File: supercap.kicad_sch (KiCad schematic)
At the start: 33 parts, among them Q1001 SS8050, Q1002 SS8050, Q1003 SS8050, U1001 LMV321-TR, U1002 LMV321-TR, U1003 LMV321-TR

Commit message: Weeded out all ERC errors
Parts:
- added C1202: 100nF, Capacitor_SMD:C_0402_1005Metric, symbol Device:C
- added C1206: CHW-2R7206R-TW, Capacitor_THT:CP_Radial_D16.0mm_P7.50mm, symbol Device:C_Polarized
- added D1202: 1N5819WS, Diode_SMD:D_SOD-323_HandSoldering, symbol Device:D_Schottky
- added Q1202: SS8050, Package_TO_SOT_SMD:SOT-23, symbol Transistor_BJT:MMBT5551L
- added R1202: 33k, Resistor_SMD:R_0402_1005Metric, symbol Device:R
- added R1208, R1220: 300k, Resistor_SMD:R_0402_1005Metric, symbol Device:R
- added R1209: 150k, Resistor_SMD:R_0402_1005Metric, symbol Device:R_Small
- added R1210: 120k, Resistor_SMD:R_0402_1005Metric, symbol Device:R_Small
- added R1219: 330k, Resistor_SMD:R_0402_1005Metric, symbol Device:R
- added U1202: LMV321-TR, Package_TO_SOT_SMD:SOT-23-5, symbol Amplifier_Operational:LMV321
- C1004, C1005, C1006: value CAS SCAP 3.0V20F -> CHW-2R7206R-TW; footprint SH-RPi:CP_Radial_D12.6mm_H26.0mm_P5.30mm_Horizontal -> Capacitor_THT:CP_Radial_D16.0mm_P7.50mm
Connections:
- net BO2-: now also R1219.2, R1220.1, U1202.3 (-)
- net BO3+: now also R1208.2, R1209.1, U1202.1 (+); no longer R1004.2, R1005.1, U1001.1 (+)
- net BO3+_: now also R1209.2, R1210.1; no longer R1005.2, R1006.1
- net BO3o: now also Q1202.1 (B), U1202.4; no longer Q1001.1 (B), U1001.4
- net SC23: now also C1202.2, C1206.2, D1202.2 (A), Q1202.2 (E), R1220.2, U1202.2 (V-); no longer C1001.2, C1004.2, D1001.2 (A), Q1001.2 (E), R1014.2, U1001.2 (V-)
- net SC23R: now also R1202.2, R1210.2; no longer R1001.2, R1006.2
- new net BO4+: R1004.2, R1005.1, U1001.1 (+)
- new net BO4+_: R1005.2, R1006.1
- new net BO4o: Q1001.1 (B), U1001.4
- new net SC34: C1001.2, C1004.2, C1202.1, C1206.1, D1001.2 (A), D1202.1 (K), Q1001.2 (E), Q1202.3 (C), R1014.2, R1208.1, U1001.2 (V-), U1202.5 (V+)
- new net SC34R: R1001.2, R1006.2, R1202.1, R1219.1
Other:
- company: Hat Labs Ltd -> Hat Labs Oy
- title: Sailor Hat for Raspberry Pi -> HALPI2
- moved on the sheet: C1001, C1002, C1003, C1004, C1005, C1006, D1001, D1002, D1003, Q1001, Q1002, Q1003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

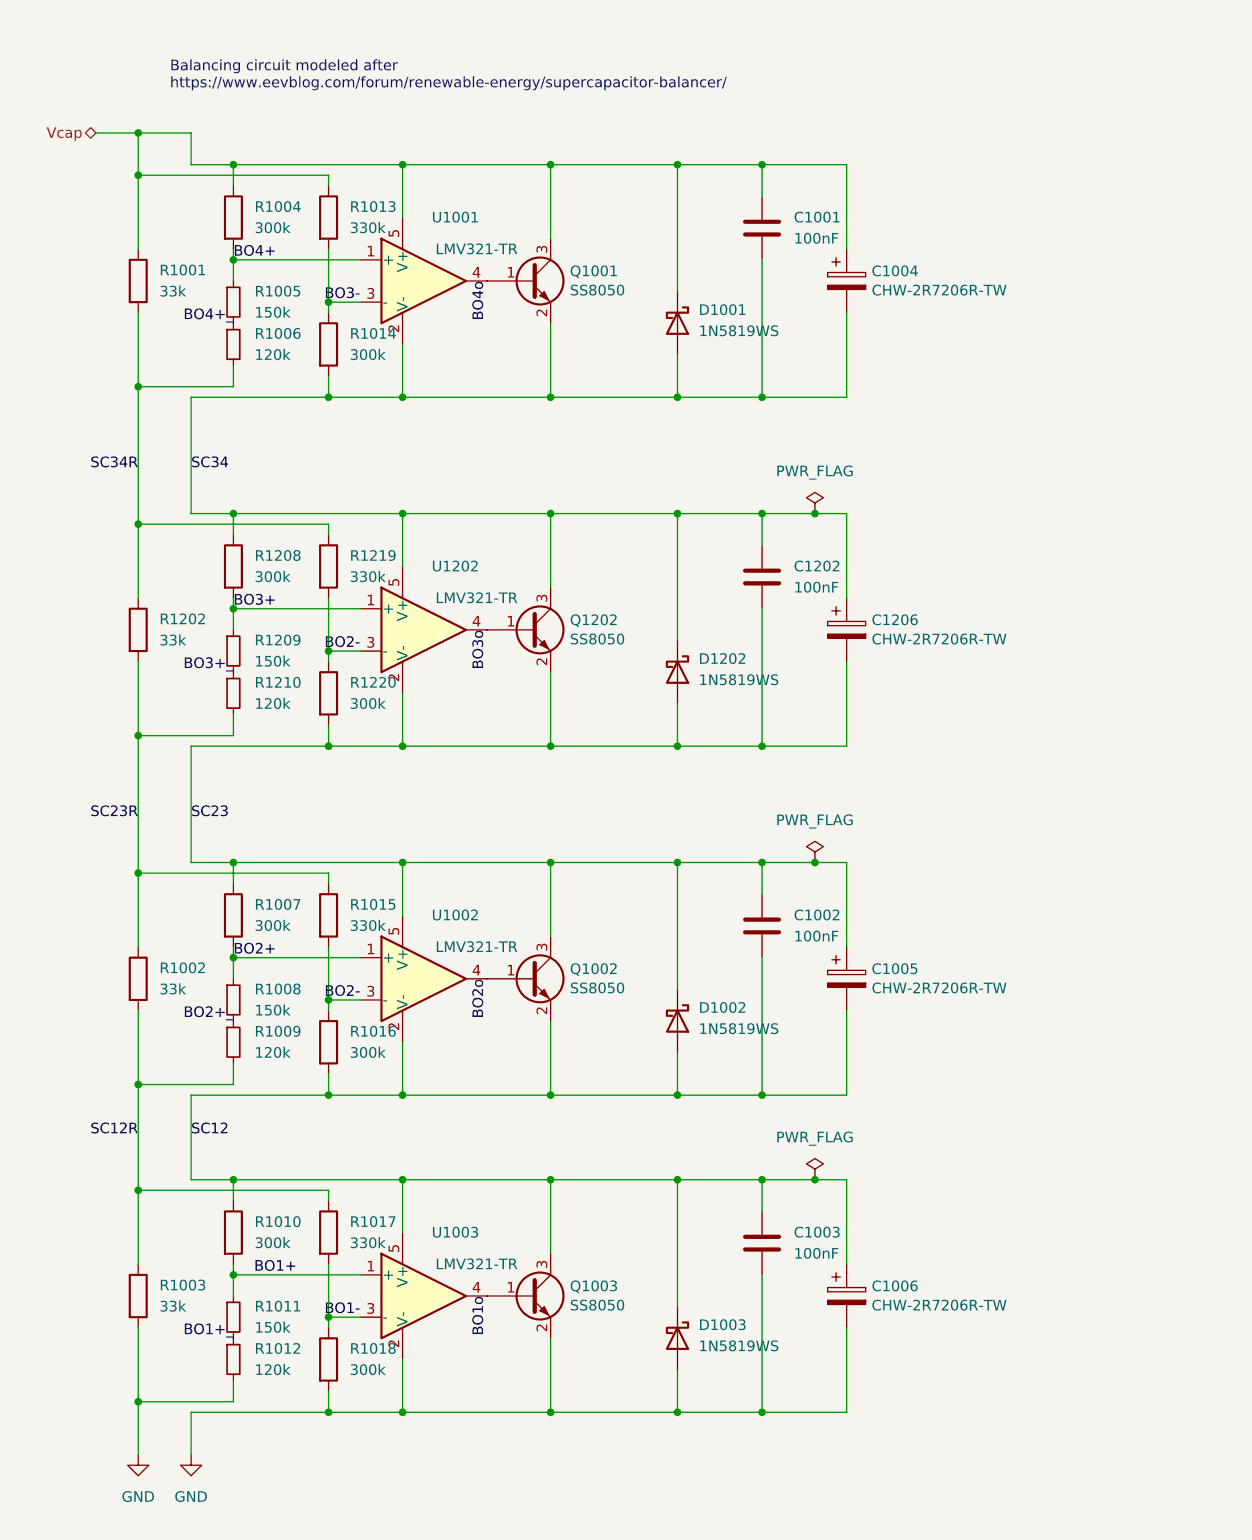
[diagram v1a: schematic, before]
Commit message: Implement ideal diodes for input and LDO power ORing
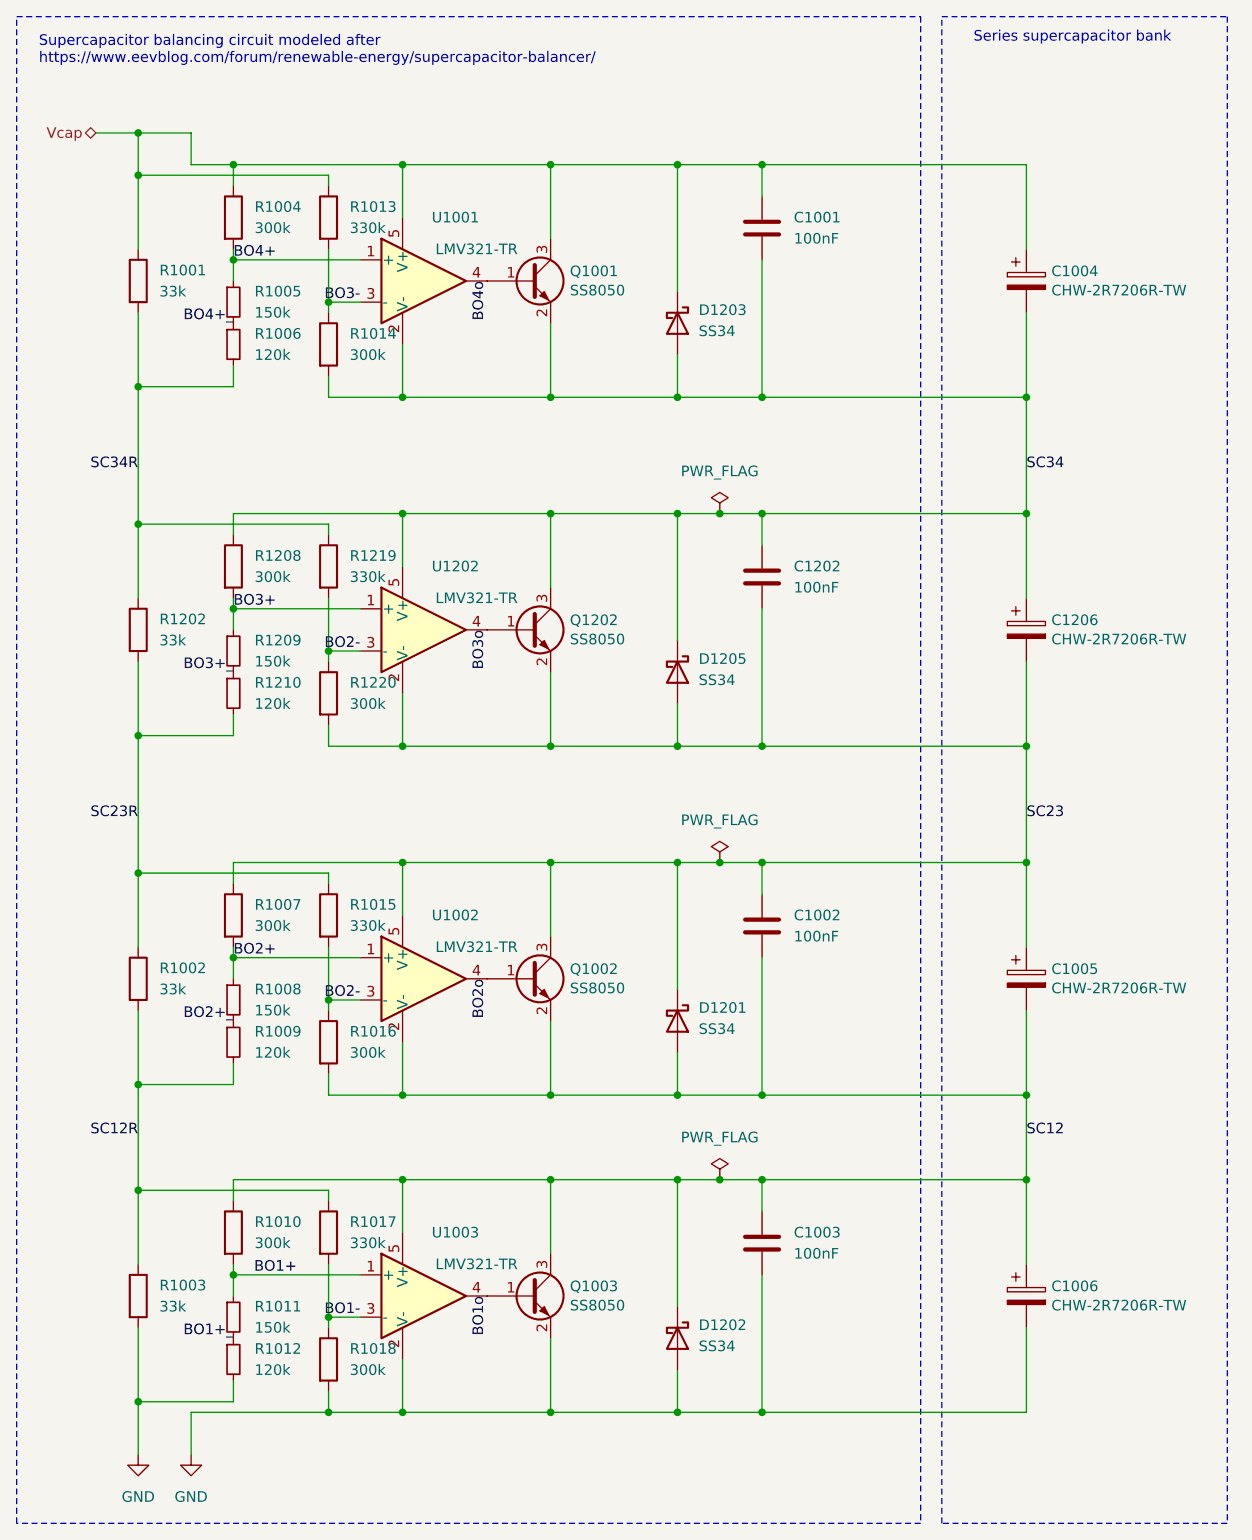
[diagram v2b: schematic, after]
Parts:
- removed D1001, D1002, D1003, D1202: 1N5819WS, Diode_SMD:D_SOD-323_HandSoldering, symbol Device:D_Schottky
- added D1201, D1202, D1203, D1205: SS34, Diode_SMD:D_SMA, symbol Diode:SS34
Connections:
- net GND: now also D1202.2 (A)
- net SC12: now also D1201.2 (A), D1202.1 (K)
- net SC23: now also D1201.1 (K), D1205.2 (A)
- net SC34: now also D1203.2 (A), D1205.1 (K)
- net Vcap: now also D1203.1 (K)
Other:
- note added: "Series supercapacitor bank"
- note added: "Supercapacitor balancing circuit modeled after https://www.eevblog.com/forum/renewable-energy/supercapacitor-balancer/"
- note removed: "Balancing circuit modeled after https://www.eevblog.com/forum/renewable-energy/supercapacitor-balancer/"
- moved on the sheet: C1004, C1005, C1006, C1206

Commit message: Re-annotate schematics
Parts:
- renumbered D1203 to D1201, D1205 to D1202, D1201 to D1203, D1202 to D1204

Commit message: Sprinkle test points on the schematics
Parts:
- added TP1201, TP1202, TP1203, TP1204: TestPoint, TestPoint:TestPoint_Pad_D1.0mm, symbol Connector:TestPoint
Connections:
- net SC12: now also TP1201.1
- net SC23: now also TP1202.1
- net SC34: now also TP1203.1
- net Vcap: now also TP1204.1

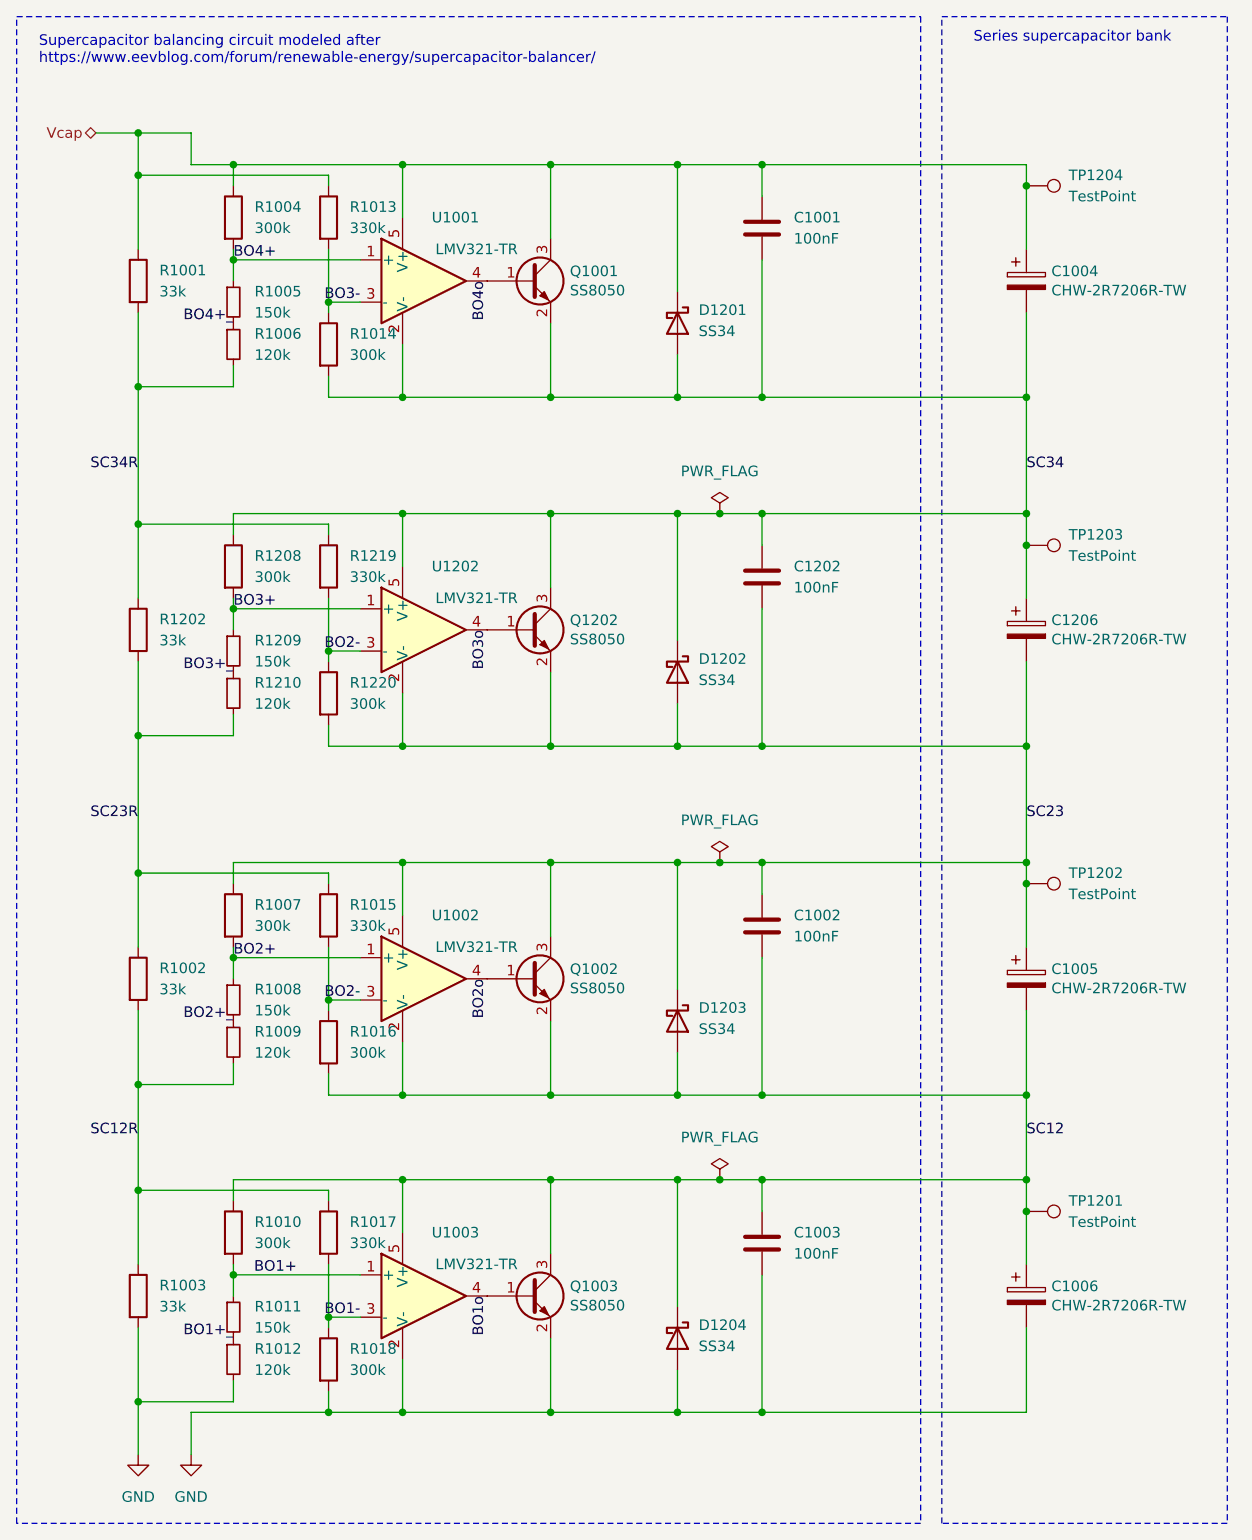
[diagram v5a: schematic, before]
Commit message: Partial trace layout, kick-ass custom rules
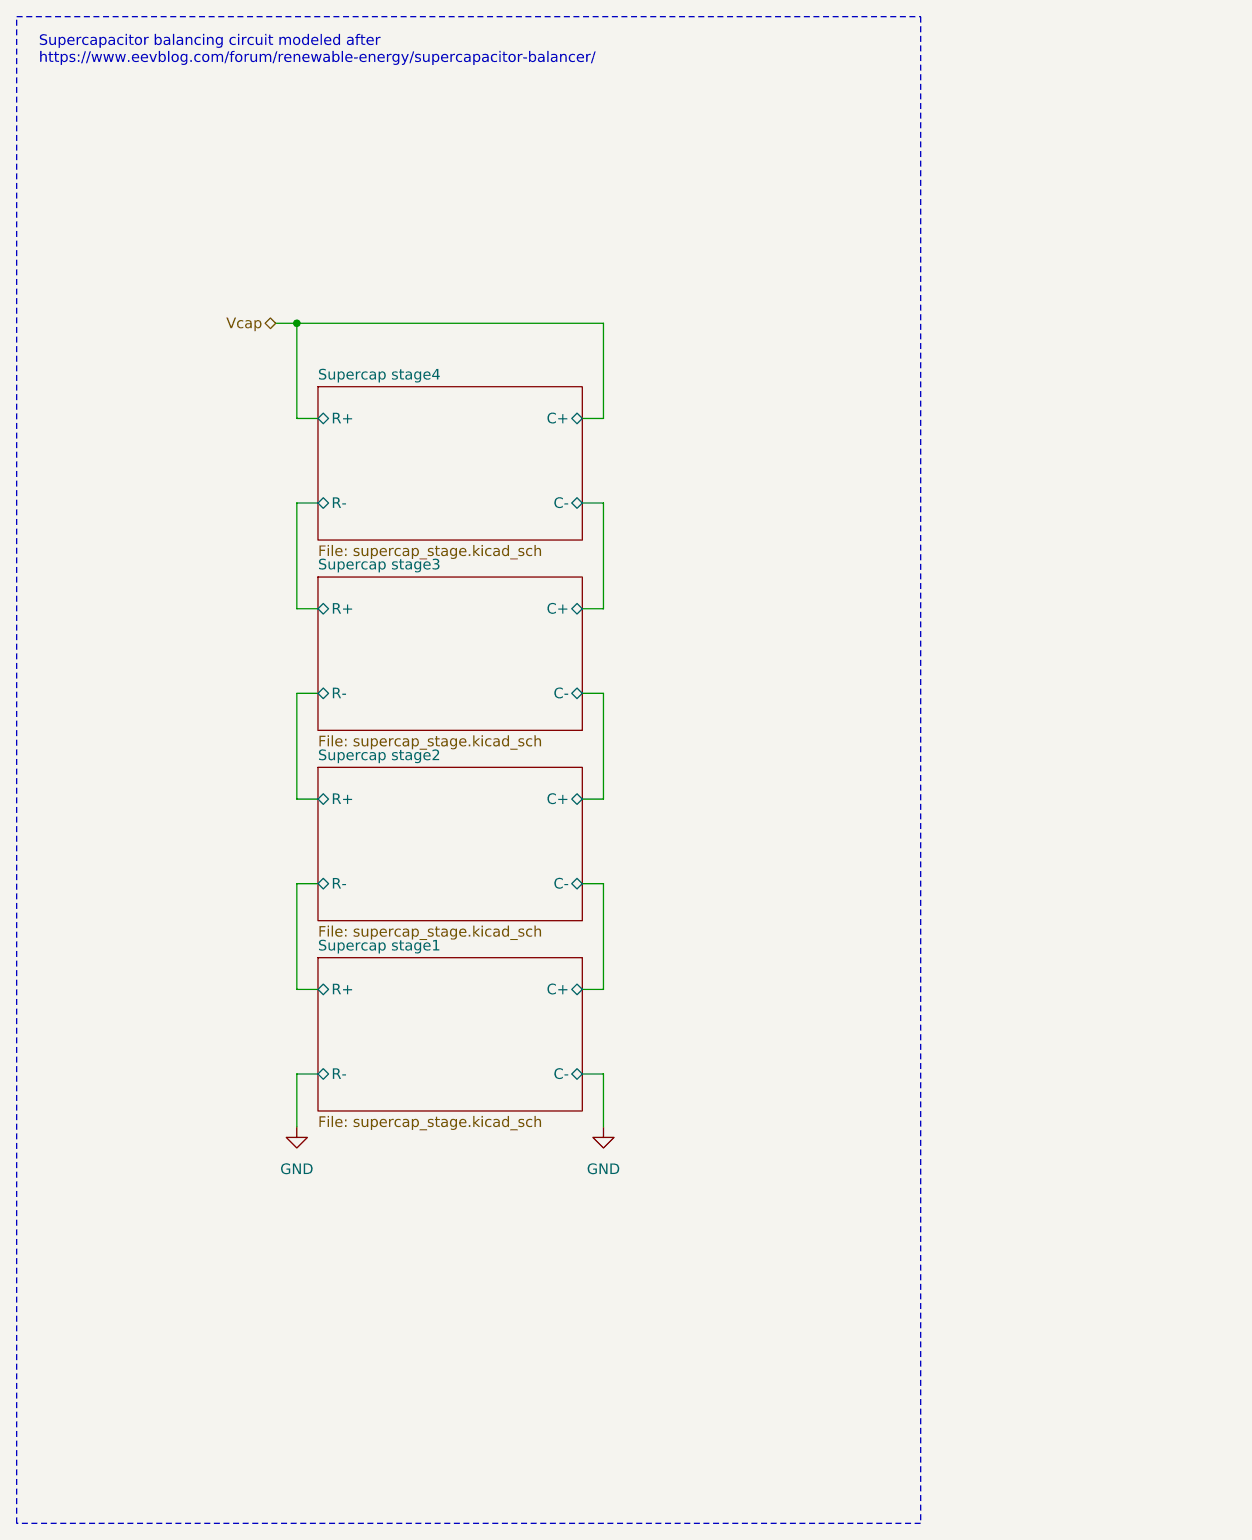
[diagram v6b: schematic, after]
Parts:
- removed C1001, C1002, C1003, C1202: 100nF, Capacitor_SMD:C_0402_1005Metric, symbol Device:C
- removed C1004, C1005, C1006, C1206: CHW-2R7206R-TW, Capacitor_THT:CP_Radial_D16.0mm_P7.50mm, symbol Device:C_Polarized
- removed D1201, D1202, D1203, D1204: SS34, Diode_SMD:D_SMA, symbol Diode:SS34
- removed Q1001, Q1002, Q1003, Q1202: SS8050, Package_TO_SOT_SMD:SOT-23, symbol Transistor_BJT:MMBT5551L
- removed R1001, R1002, R1003, R1202: 33k, Resistor_SMD:R_0402_1005Metric, symbol Device:R
- removed R1004, R1007, R1010, R1014, R1016, R1018, R1208, R1220: 300k, Resistor_SMD:R_0402_1005Metric, symbol Device:R
- removed R1005, R1008, R1011, R1209: 150k, Resistor_SMD:R_0402_1005Metric, symbol Device:R_Small
- removed R1006, R1009, R1012, R1210: 120k, Resistor_SMD:R_0402_1005Metric, symbol Device:R_Small
- removed R1013, R1015, R1017, R1219: 330k, Resistor_SMD:R_0402_1005Metric, symbol Device:R
- removed TP1201, TP1202, TP1203, TP1204: TestPoint, TestPoint:TestPoint_Pad_D1.0mm, symbol Connector:TestPoint
- removed U1001, U1002, U1003, U1202: LMV321-TR, Package_TO_SOT_SMD:SOT-23-5, symbol Amplifier_Operational:LMV321
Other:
- added sheet Supercap stage1 (supercap_stage.kicad_sch)
- added sheet Supercap stage2 (supercap_stage.kicad_sch)
- added sheet Supercap stage3 (supercap_stage.kicad_sch)
- added sheet Supercap stage4 (supercap_stage.kicad_sch)
- note removed: "Series supercapacitor bank"
